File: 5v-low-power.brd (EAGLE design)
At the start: 68.6 x 40.3 mm, 37 parts, among them J1 Bypass, J2 En, J3 12v, J4 5V Out, J5 LED EN, J6 POWERPOLE_POWER25A, J7 POWERPOLE_POWER25A, Q1 SI4532ADY, U1 LT1934ES6TRMPBF

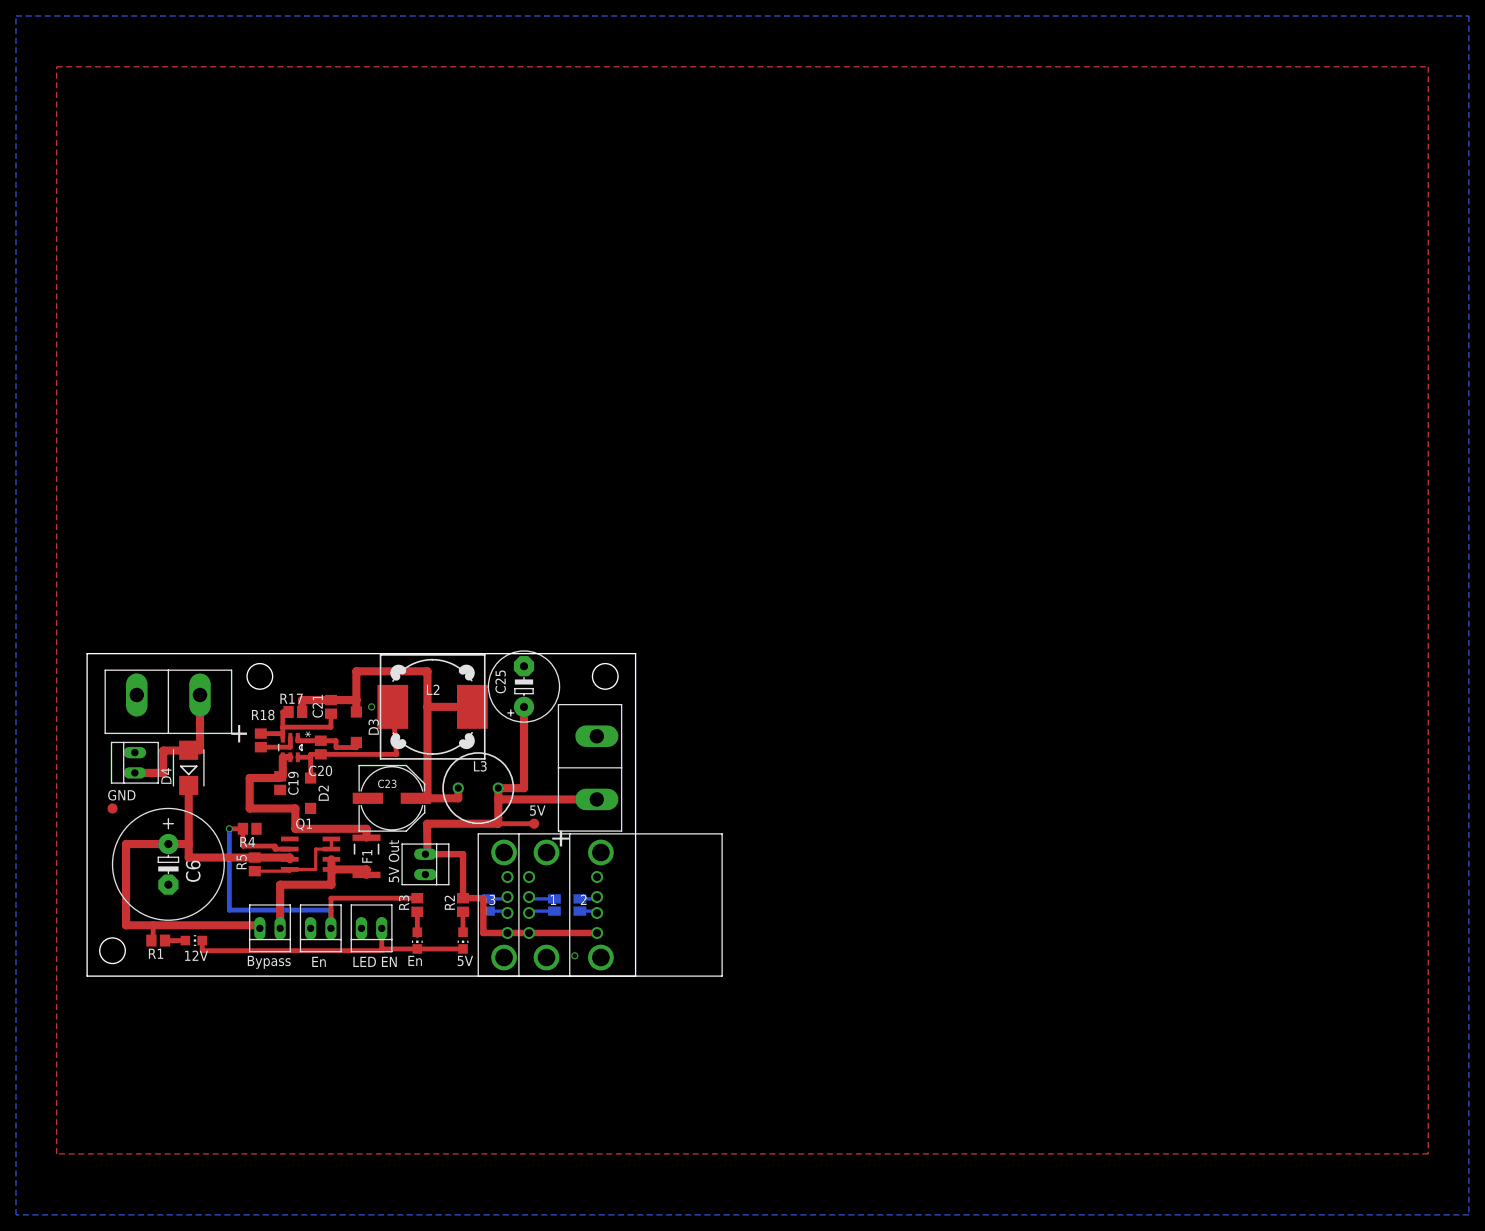
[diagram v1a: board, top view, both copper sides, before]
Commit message: Added more smoothing caps
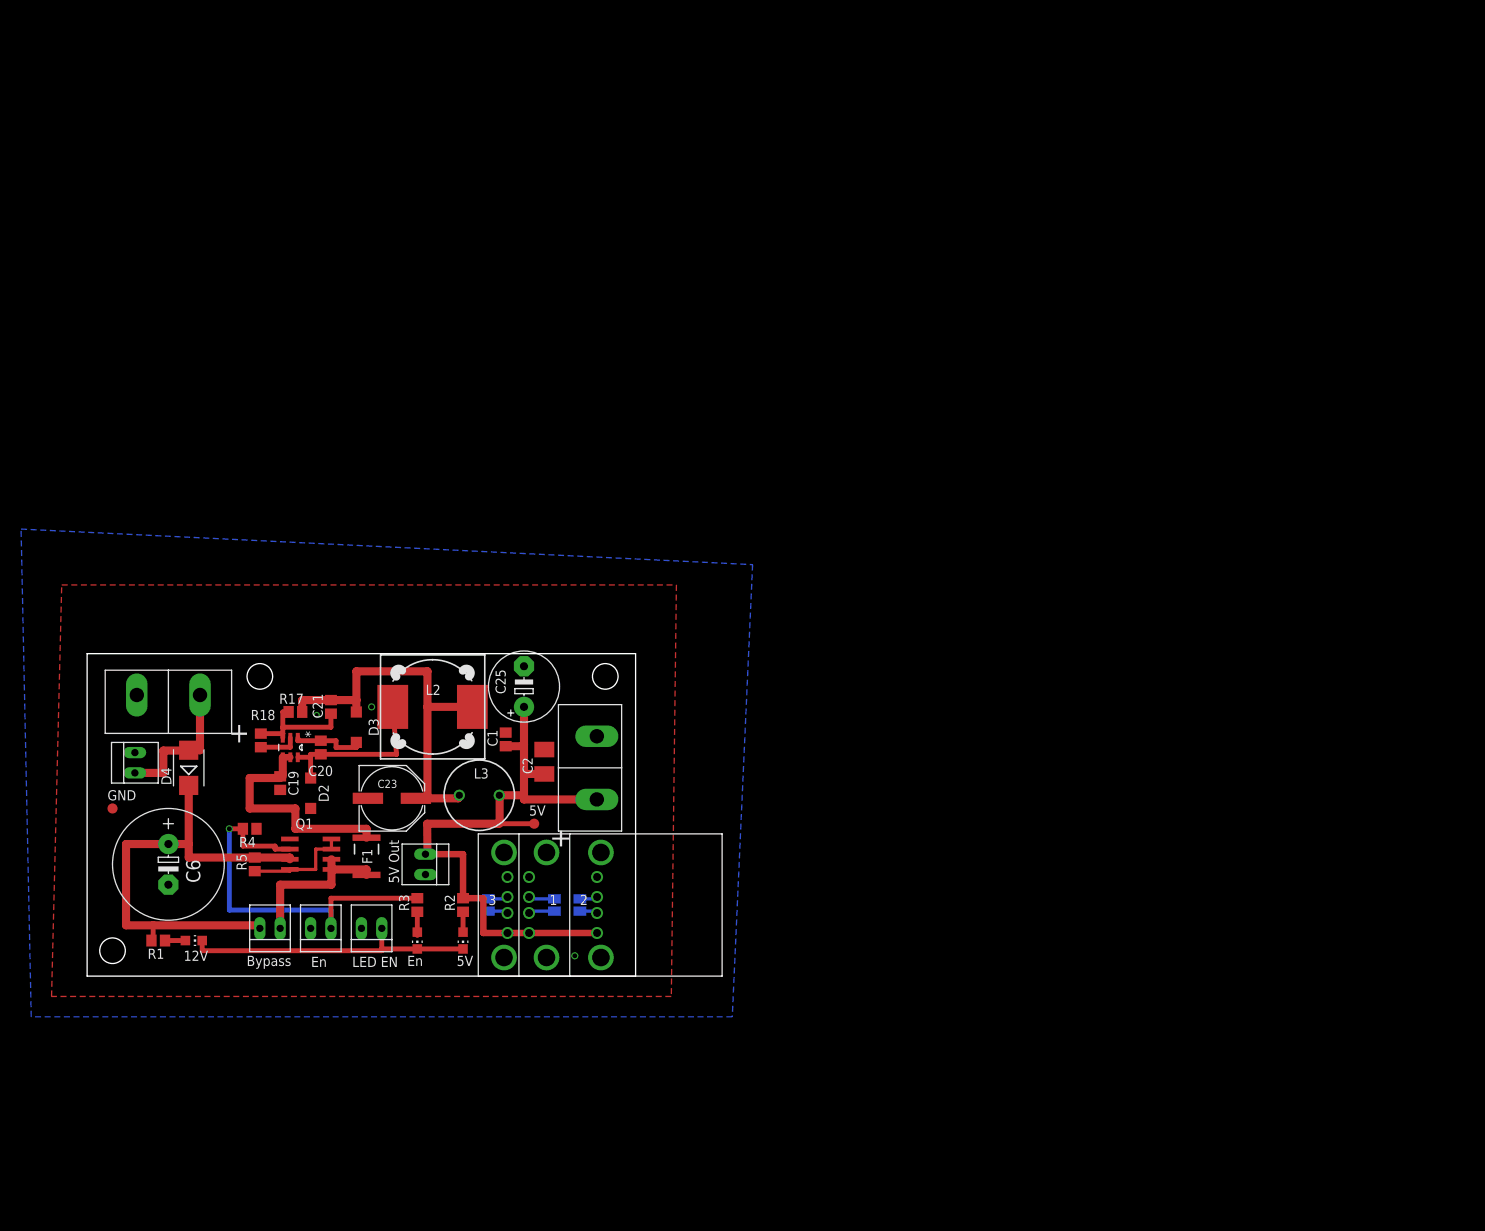
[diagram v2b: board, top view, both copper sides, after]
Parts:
- added C1: (no value), resistor:C0805
- added C2: (no value), resistor:B/3528-21R
- moved L3 0.90 mm to (49.0, 22.6)
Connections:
- net 5V: now also C1.1, C2.+
- net GND: now also C1.2, C2.-
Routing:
- net N$107: track 50.3 -> 49.4 mm
- net 5V: track 80.0 -> 80.7 mm
- net GND: vias 2 -> 3
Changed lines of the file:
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@@
 <setting verticaltext="up"/>
 </settings>
-<grid distance="25" unitdist="mil" unit="mil" style="lines" multiple="1" display="yes" altdistance="5" altunitdist="mil" altunit="mm"/>
+<grid distance="5" unitdist="mil" unit="mil" style="lines" multiple="1" display="yes" altdistance="5" altunitdist="mil" altunit="mm"/>
 <layers>
 <layer number="1" name="Top" color="4" fill="1" visible="yes" active="yes"/>
@@
 <attribute name="NAME" x="36.465" y="30.015" size="1.27" layer="25" rot="R90"/>
 </element>
-<element name="L3" library="rcl" package="6000-XXXX-RC" value="20uH" x="48.895" y="23.495" smashed="yes">
-<attribute name="NAME" x="48.1994" y="25.5876" size="1.27" layer="25"/>
-<attribute name="VALUE" x="46.9294" y="20.2594" size="1.27" layer="27"/>
+<element name="L3" library="rcl" package="6000-XXXX-RC" value="20uH" x="49.022" y="22.606" smashed="yes">
+<attribute name="NAME" x="48.3264" y="24.6986" size="1.27" layer="25"/>
+<attribute name="VALUE" x="47.0564" y="19.3704" size="1.27" layer="27"/>
 </element>
 <element name="C25" library="rcl" package="E5-8,5" value="330uF" x="54.61" y="36.195" smashed="yes" rot="R90">
@@
 <element name="SJ2" library="jumper" package="SJ" value="" x="61.595" y="8.89" rot="MR90"/>
 <element name="SJ3" library="jumper" package="SJ" value="" x="50.165" y="8.89" rot="MR90"/>
+<element name="C1" library="resistor" package="C0805" value="" x="52.324" y="29.591" rot="R90"/>
+<element name="C2" library="resistor" package="B/3528-21R" value="" x="57.15" y="26.797" smashed="yes" rot="R270">
+<attribute name="NAME" x="54.432" y="27.35" size="1.27" layer="25" rot="R270"/>
+<attribute name="VALUE" x="54.225" y="28.747" size="1.27" layer="27" rot="R270"/>
+</element>
 </elements>
 <signals>
@@
 <contactref element="J7" pad="BLACK"/>
 <polygon width="0.6096" layer="16">
-<vertex x="-8.89" y="120.015"/>
-<vertex x="172.72" y="120.015"/>
-<vertex x="172.72" y="-29.845"/>
-<vertex x="-8.89" y="-29.845"/>
+<vertex x="-8.255" y="55.88"/>
+<vertex x="83.185" y="51.435"/>
+<vertex x="80.645" y="-5.08"/>
+<vertex x="-6.985" y="-5.08"/>
 </polygon>
 <polygon width="0.6096" layer="1">
-<vertex x="-3.81" y="113.665"/>
-<vertex x="167.64" y="113.665"/>
-<vertex x="167.64" y="-22.225"/>
-<vertex x="-3.81" y="-22.225"/>
+<vertex x="-3.175" y="48.895"/>
+<vertex x="73.66" y="48.895"/>
+<vertex x="73.025" y="-2.54"/>
+<vertex x="-4.445" y="-2.54"/>
 </polygon>
 <contactref element="C19" pad="2"/>
@@
 <contactref element="U$1" pad="P3.4"/>
 <via x="60.96" y="2.54" extent="1-16" drill="0.6"/>
+<contactref element="C2" pad="-"/>
+<contactref element="C1" pad="2"/>
+<via x="28.702" y="32.639" extent="1-16" drill="0.4826"/>
 </signal>
 <signal name="VCC">
@@
 <wire x1="41.1" y1="22.225" x2="42.545" y2="22.225" width="1.016" layer="1"/>
 <wire x1="42.545" y1="22.225" x2="46.395" y2="22.225" width="1.016" layer="1"/>
-<wire x1="46.395" y1="22.225" x2="46.395" y2="23.495" width="1.016" layer="1"/>
+<wire x1="46.395" y1="22.225" x2="46.522" y2="22.606" width="1.016" layer="1"/>
 </signal>
 <signal name="VCC_HP2_SW">
@@
 <contactref element="J4" pad="2"/>
 <contactref element="J6" pad="RED"/>
-<wire x1="51.395" y1="23.495" x2="54.61" y2="23.495" width="1.016" layer="1"/>
-<wire x1="54.61" y1="23.495" x2="54.61" y2="33.655" width="1.016" layer="1"/>
+<wire x1="54.61" y1="22.606" x2="54.61" y2="25.272" width="1.016" layer="1"/>
+<wire x1="54.61" y1="25.272" x2="54.61" y2="28.956" width="1.016" layer="1"/>
+<wire x1="54.61" y1="28.956" x2="54.61" y2="33.655" width="1.016" layer="1"/>
 <wire x1="42.291" y1="15.24" x2="42.545" y2="15.24" width="1.016" layer="1"/>
 <wire x1="42.545" y1="15.24" x2="42.505" y2="19.05" width="1.016" layer="1"/>
 <wire x1="42.505" y1="19.05" x2="51.395" y2="19.05" width="1.016" layer="1"/>
-<wire x1="51.395" y1="19.05" x2="51.395" y2="23.495" width="1.016" layer="1"/>
 <wire x1="46.99" y1="9.74" x2="49.53" y2="9.74" width="0.8128" layer="1"/>
 <wire x1="49.53" y1="9.74" x2="49.53" y2="9.525" width="0.6096" layer="1"/>
-<wire x1="55.88" y1="19.05" x2="51.395" y2="19.05" width="0.6096" layer="1"/>
+<wire x1="55.88" y1="19.05" x2="51.562" y2="19.05" width="0.6096" layer="1"/>
 <contactref element="U$1" pad="P1.1"/>
 <contactref element="U$1" pad="P2.1"/>
 <contactref element="U$1" pad="P3.1"/>
+<wire x1="51.562" y1="19.05" x2="51.395" y2="19.05" width="0.6096" layer="1"/>
 <wire x1="42.545" y1="15.24" x2="46.99" y2="15.24" width="0.8128" layer="1"/>
 <wire x1="46.99" y1="15.24" x2="46.99" y2="9.74" width="0.8128" layer="1"/>
@@
 <wire x1="52.545" y1="5.39" x2="49.53" y2="5.39" width="0.8128" layer="1"/>
 <wire x1="49.53" y1="5.39" x2="49.53" y2="9.525" width="0.8128" layer="1"/>
-<wire x1="63.715" y1="22.085" x2="51.395" y2="22.085" width="1.016" layer="1"/>
-<wire x1="51.395" y1="22.085" x2="51.395" y2="23.495" width="0.8128" layer="1"/>
+<contactref element="C2" pad="+"/>
+<contactref element="C1" pad="1"/>
+<wire x1="57.15" y1="25.272" x2="54.61" y2="25.272" width="1.016" layer="1"/>
+<wire x1="52.324" y1="28.741" x2="54.395" y2="28.741" width="1.016" layer="1"/>
+<wire x1="54.395" y1="28.741" x2="54.61" y2="28.956" width="1.016" layer="1"/>
+<wire x1="51.522" y1="22.606" x2="51.562" y2="22.606" width="1.016" layer="1"/>
+<wire x1="51.562" y1="22.606" x2="54.61" y2="22.606" width="1.016" layer="1"/>
+<wire x1="63.715" y1="22.085" x2="54.61" y2="22.085" width="1.016" layer="1"/>
+<wire x1="54.61" y1="22.085" x2="54.61" y2="22.606" width="1.016" layer="1"/>
+<wire x1="51.562" y1="22.606" x2="51.562" y2="19.05" width="1.016" layer="1"/>
 </signal>
 <signal name="LEDGND1">
